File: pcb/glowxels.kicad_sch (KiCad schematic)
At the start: 83 parts, among them J1 OUT, J2 IN, U1 STP16CPC26, U2 STP16CPC26, U3 STP16CPC26, U4 STP16CPC26

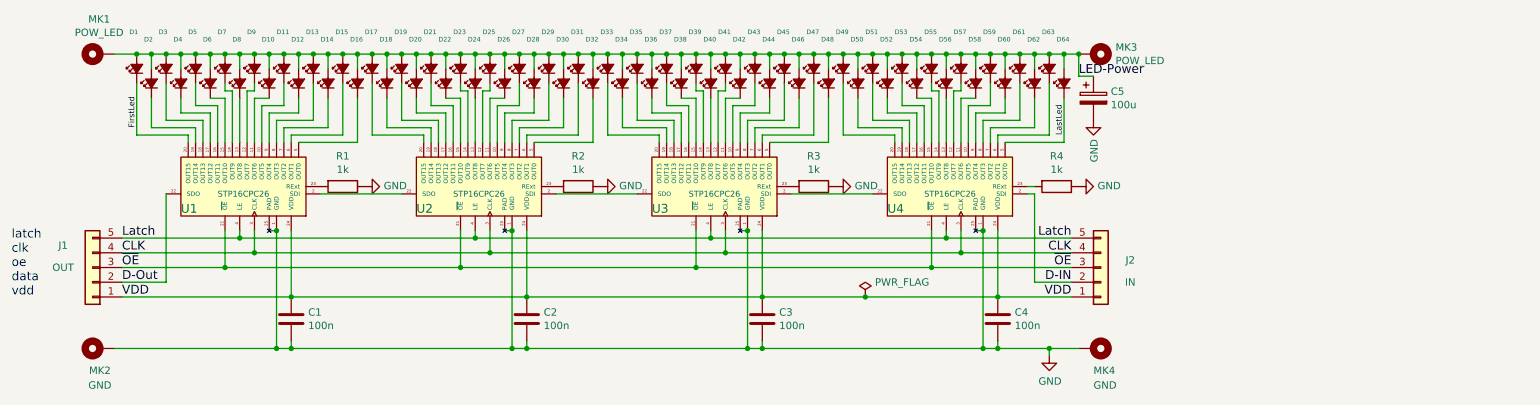
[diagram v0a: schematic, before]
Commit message: Start board. Manually placed some LEDs.
But hopefully this can be improved with a little script.
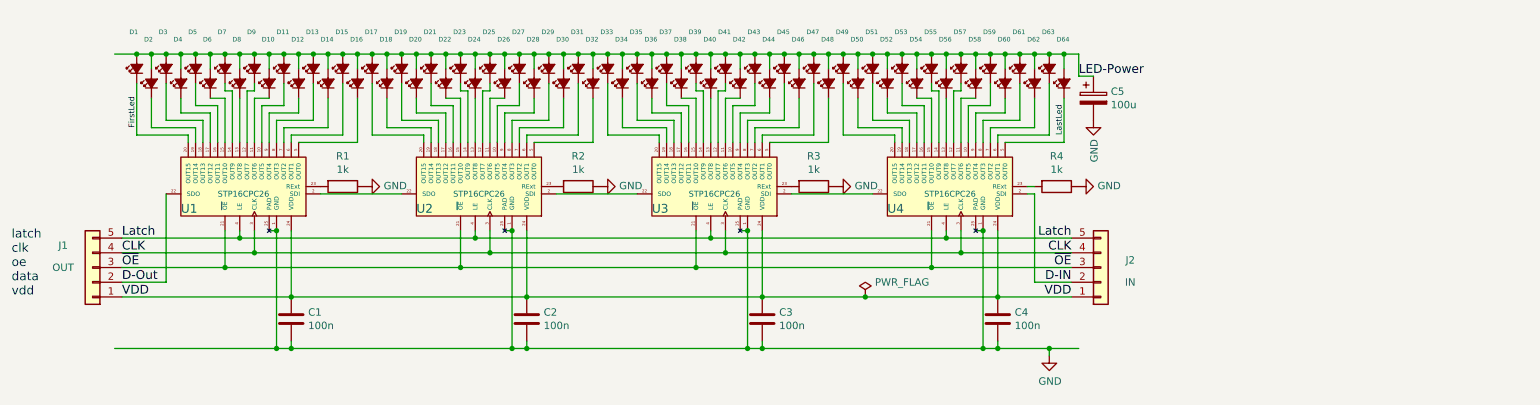
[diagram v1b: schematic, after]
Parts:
- removed MK1, MK3: POW_LED, Mounting_Holes:MountingHole_2.7mm_M2.5_DIN965_Pad, symbol Mechanical:MountingHole_Pad
- removed MK2, MK4: GND, Mounting_Holes:MountingHole_2.7mm_M2.5_DIN965_Pad, symbol Mechanical:MountingHole_Pad
- D1, D10, D11, D12, D13, D14, D15, D16, D17, D18, D19, D2, D20, D21, D22, D23, D24, D25, D26, D27, D28, D29, D3, D30, D31, D32, D33, D34, D35, D36, D37, D38, D39, D4, D40, D41, D42, D43, D44, D45, D46, D47, D48, D49, D5, D50, D51, D52, D53, D54, D55, D56, D57, D58, D59, D6, D60, D61, D62, D63, D64, D7, D8, D9: footprint Glowxels:LED_1210 -> LED_SMD:LED_0603_1608Metric

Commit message: First version, fully routed.
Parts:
- removed C5: 100u, Capacitor_SMD:CP_Elec_6.3x5.3, symbol Device:CP
- removed J1: OUT, Glowxels:EdgeConnect, symbol Connector_Generic:Conn_01x05
- removed J2: IN, Glowxels:EdgeConnect, symbol Connector_Generic:Conn_01x05
- added C10, C11, C12, C5, C6, C7, C8, C9: 47u, Capacitor_SMD:C_1210_3225Metric, symbol Device:C
- added J1: Conn_01x06_Pin, Connector_PinHeader_2.00mm:PinHeader_1x06_P2.00mm_Vertical, symbol Connector:Conn_01x06_Pin
- added J2: Conn_01x02_Pin, Connector_PinHeader_2.00mm:PinHeader_1x02_P2.00mm_Vertical, symbol Connector:Conn_01x02_Pin
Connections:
- net CLK: now also J1.3 (Pin_3)
- net D-IN: now also J1.4 (Pin_4)
- net GND: now also C10.2, C11.2, C12.2, C5.2, C6.2, C7.2, C8.2, C9.2, J1.1 (Pin_1), J2.1 (Pin_1)
- net LED-Power: now also C10.1, C11.1, C12.1, C5.1, C6.1, C7.1, C8.1, C9.1, J2.2 (Pin_2)
- net Latch: now also J1.2 (Pin_2)
- net VDD: now also J1.5 (Pin_5)
- net ~{OE}: now also J1.6 (Pin_6)
